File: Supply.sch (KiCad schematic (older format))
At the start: 22 parts, among them IC2 TPS65320C

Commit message: - updated project to 5.0.0 - added ignore file
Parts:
- B1: symbol MTC1 -> HSWR-V2-rescue:MTC1
- C27, C28, C30, C31, C32, C45, C46, C47, C48: symbol C -> Device:C
- C29, C49: symbol CP -> Device:CP
- D8, D9: symbol D_Schottky -> Device:D_Schottky
- IC2: symbol TPS65320C -> HSWR-V2-rescue:TPS65320C
- L1: symbol INDUCTOR -> HSWR-V2-rescue:INDUCTOR
- R39, R40, R41, R42, R43, R44: symbol R -> Device:R
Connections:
- wire segments 30 -> 38
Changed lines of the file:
@@
-EESchema Schematic File Version 2
-LIBS:HSWR V2-rescue
-LIBS:power
-LIBS:device
-LIBS:transistors
-LIBS:conn
-LIBS:linear
-LIBS:regul
-LIBS:74xx
-LIBS:cmos4000
-LIBS:adc-dac
-LIBS:memory
-LIBS:xilinx
-LIBS:microcontrollers
-LIBS:dsp
-LIBS:microchip
-LIBS:analog_switches
-LIBS:motorola
-LIBS:texas
-LIBS:intel
-LIBS:audio
-LIBS:interface
-LIBS:digital-audio
-LIBS:philips
-LIBS:display
-LIBS:cypress
-LIBS:siliconi
-LIBS:opto
-LIBS:atmel
-LIBS:contrib
-LIBS:valves
+EESchema Schematic File Version 4
 LIBS:HSWR V2-cache
-EELAYER 25 0
+EELAYER 26 0
 EELAYER END
 $Descr A4 11693 8268
@@
 $EndDescr
 $Comp
-L C C28
+L Device:C C28
 U 1 1 5757C618
 P 3350 3100
@@
 	3350 2800 3350 2950
 $Comp
-L GND #PWR052
+L power:GND #PWR052
 U 1 1 5757C686
 P 3350 3250
@@
 $EndComp
 $Comp
-L +12V #PWR053
+L power:+12V #PWR053
 U 1 1 5757C6C9
 P 3350 2800
@@
 Connection ~ 3350 2950
 $Comp
-L MTC1 B1
+L HSWR-V2-rescue:MTC1 B1
 U 1 1 5759A0C2
 P 2300 3150
@@
 $EndComp
 $Comp
-L +12VA #PWR054
+L power:+12VA #PWR054
 U 1 1 5759A1BD
 P 1350 2800
@@
 $EndComp
 Wire Wire Line
-	1350 2800 1350 3000
+	1350 2800 1350 2950
 Wire Wire Line
 	1350 2950 1650 2950
 $Comp
-L Earth #PWR055
+L power:Earth #PWR055
 U 1 1 5759A43B
 P 1350 3500
@@
 $EndComp
 Wire Wire Line
-	1350 3300 1350 3500
+	1350 3300 1350 3350
 Wire Wire Line
 	1350 3350 1650 3350
 $Comp
-L C C27
+L Device:C C27
 U 1 1 5759AB81
 P 1350 3150
@@
 Connection ~ 1350 3350
 $Comp
-L GND #PWR056
+L power:GND #PWR056
 U 1 1 5759B7CF
 P 2950 3350
@@
 $EndComp
 $Comp
-L TPS65320C IC2
+L HSWR-V2-rescue:TPS65320C IC2
 U 1 1 589B5162
 P 5100 3500
@@
 $EndComp
 $Comp
-L C C30
+L Device:C C30
 U 1 1 589B52B3
 P 3950 3100
@@
 $EndComp
 $Comp
-L CP C29
+L Device:CP C29
 U 1 1 589B52D8
 P 3650 3100
@@
 $EndComp
 Wire Wire Line
-	2950 2950 4350 2950
-Wire Wire Line
-	3350 3250 3350 3250
+	2950 2950 3350 2950
 Connection ~ 3950 2950
 Connection ~ 3650 2950
 $Comp
-L GND #PWR057
+L power:GND #PWR057
 U 1 1 589B5534
 P 3650 3250
@@
 $EndComp
 $Comp
-L GND #PWR058
+L power:GND #PWR058
 U 1 1 589B5551
 P 3950 3250
@@
 $EndComp
 Wire Wire Line
-	4350 2950 4350 3450
+	4350 2950 4350 3300
 Connection ~ 4350 3300
 Connection ~ 4350 2950
 $Comp
-L R R39
+L Device:R R39
 U 1 1 589B5713
 P 3900 4250
@@
 $EndComp
 $Comp
-L C C31
+L Device:C C31
 U 1 1 589B5758
 P 4150 4250
@@
 	3900 3950 3900 4100
 $Comp
-L GND #PWR059
+L power:GND #PWR059
 U 1 1 589B57C2
 P 3900 4400
@@
 $EndComp
 $Comp
-L GND #PWR060
+L power:GND #PWR060
 U 1 1 589B57E5
 P 4150 4400
@@
 $EndComp
 $Comp
-L GND #PWR061
+L power:GND #PWR061
 U 1 1 589B58C3
 P 4900 4400
@@
 $EndComp
 $Comp
-L GND #PWR062
+L power:GND #PWR062
 U 1 1 589B58E6
 P 5300 4400
@@
 $EndComp
 $Comp
-L R R42
+L Device:R R42
 U 1 1 589B5963
 P 6350 4100
@@
 $EndComp
 $Comp
-L R R41
+L Device:R R41
 U 1 1 589B59A7
 P 6200 4250
@@
 $EndComp
 $Comp
-L GND #PWR063
+L power:GND #PWR063
 U 1 1 589B5AA4
 P 6200 4400
@@
 	1    0    0    -1
 $EndComp
-Wire Wire Line
-	6200 4400 6200 4400
 Connection ~ 6200 4100
 Wire Wire Line
@@
 	6500 3750 6500 4100
 $Comp
-L C C47
+L Device:C C47
 U 1 1 589B5CE1
 P 6500 4250
@@
 $EndComp
 $Comp
-L GND #PWR064
+L power:GND #PWR064
 U 1 1 589B5D3A
 P 6500 4400
@@
 Connection ~ 6500 4100
 $Comp
-L +3V3 #PWR065
+L power:+3V3 #PWR065
 U 1 1 589B5D71
 P 6650 4100
@@
 $EndComp
 $Comp
-L R R40
+L Device:R R40
 U 1 1 589B6017
 P 6100 3500
@@
 $EndComp
 $Comp
-L C C45
+L Device:C C45
 U 1 1 589B6055
 P 6100 3650
@@
 $EndComp
 $Comp
-L C C46
+L Device:C C46
 U 1 1 589B6319
 P 6400 3500
@@
 Connection ~ 5850 3500
 $Comp
-L GND #PWR066
+L power:GND #PWR066
 U 1 1 589B655F
 P 6550 3500
@@
 $EndComp
 $Comp
-L R R43
+L Device:R R43
 U 1 1 589B6AE0
 P 7150 3400
@@
 $EndComp
 $Comp
-L R R44
+L Device:R R44
 U 1 1 589B6BD8
 P 7300 3250
@@
 $EndComp
 $Comp
-L GND #PWR067
+L power:GND #PWR067
 U 1 1 589B6C41
 P 7150 3550
@@
 	5850 3250 7150 3250
 $Comp
-L C C48
+L Device:C C48
 U 1 1 589B6CE4
 P 7450 3400
@@
 $EndComp
 $Comp
-L GND #PWR068
+L power:GND #PWR068
 U 1 1 589B6D8B
 P 7450 3550
@@
 $EndComp
 $Comp
-L GND #PWR069
+L power:GND #PWR069
 U 1 1 589B6DCC
 P 7700 3550
@@
 Connection ~ 7450 3250
 $Comp
-L D_Schottky D9
+L Device:D_Schottky D9
 U 1 1 589B7102
 P 6900 3450
@@
 $EndComp
 $Comp
-L GND #PWR070
+L power:GND #PWR070
 U 1 1 589B715E
 P 6900 3600
@@
 $EndComp
 Wire Wire Line
-	5850 3100 7000 3100
-$Comp
-L INDUCTOR L1
+	5850 3100 6150 3100
+$Comp
+L HSWR-V2-rescue:INDUCTOR L1
 U 1 1 589B8AC8
 P 7300 3100
@@
 $EndComp
 $Comp
-L C C32
+L Device:C C32
 U 1 1 589B8B47
 P 6000 2950
@@
 	6500 4100 6650 4100
 Wire Wire Line
-	7700 2500 7700 3250
+	7700 2500 7700 2600
 Wire Wire Line
 	6900 3300 6900 3100
@@
 Connection ~ 7700 3250
 $Comp
-L +5V #PWR071
+L power:+5V #PWR071
 U 1 1 589BAA8C
 P 7700 2500
@@
 Connection ~ 7700 2600
 $Comp
-L D_Schottky D8
+L Device:D_Schottky D8
 U 1 1 589BBCFD
 P 5850 4250
@@
 NRST
 $Comp
-L CP C49
+L Device:CP C49
 U 1 1 589C2A67
 P 7700 3400
@@
 Wire Wire Line
 	7600 3100 7700 3100
+Wire Wire Line
+	3350 2950 3650 2950
+Wire Wire Line
+	1350 2950 1350 3000
+Wire Wire Line
+	1350 3350 1350 3500
+Wire Wire Line
+	3950 2950 4350 2950
+Wire Wire Line
+	3650 2950 3950 2950
+Wire Wire Line
+	4350 3300 4350 3450
+Wire Wire Line
+	6150 3100 6900 3100
+Wire Wire Line
+	6900 3100 7000 3100
+Wire Wire Line
+	7700 3100 7700 3250
+Wire Wire Line
+	7700 2600 7700 3100
 $EndSCHEMATC

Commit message: - updated to VESC6 architecture - still some things to do in schematic
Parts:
- removed B1: MTC1, alexmod:MTC1, symbol HSWR-V2-rescue:MTC1
- removed C27, C28: 22u, Capacitors_SMD:C_1206, symbol Device:C
- removed C29: 100u 16V, Capacitors_ThroughHole:C_Radial_D6.3_L11.2_P2.5, symbol Device:CP
- removed C30, C47, C48: 10u, Capacitors_SMD:C_0805, symbol Device:C
- removed C31: 3n3, Capacitors_SMD:C_0805, symbol Device:C
- removed C32: 100n, Capacitors_SMD:C_0805, symbol Device:C
- removed C45: 10p, Capacitors_SMD:C_0805, symbol Device:C
- removed C46: 5n6, Capacitors_SMD:C_0805, symbol Device:C
- removed C49: 100u 6V3, Capacitors_ThroughHole:C_Radial_D6.3_L11.2_P2.5, symbol Device:CP
- removed D8, D9: D_Schottky, Diodes_SMD:SMA_Standard, symbol Device:D_Schottky
- removed IC2: TPS65320C, alexmod:TSSOP-14_4.4x5mm_Pitch0.65mm_EP, symbol HSWR-V2-rescue:TPS65320C
- removed L1: SRR6038-3R3Y, alexmod:SRR6038, symbol HSWR-V2-rescue:INDUCTOR
- removed R39: 52k3, Resistors_SMD:R_0805, symbol Device:R
- removed R40: 28k, Resistors_SMD:R_0805, symbol Device:R
- removed R41: 30k1, Resistors_SMD:R_0805, symbol Device:R
- removed R42, R44: 95k3, Resistors_SMD:R_0805, symbol Device:R
- removed R43: 18k2, Resistors_SMD:R_0805, symbol Device:R
- added NT1: Net-Tie_2, NetTie:NetTie-3_SMD_Pad0.5mm, symbol Device:Net-Tie_2
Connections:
- net labels added: GNDPWR
- net labels removed: +12V, +12VA, +3V3, +5V, Earth, NRST
- wire segments 38 -> 0

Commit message: - layout pretty much finished except PSU and maaaaybe R2D - started work on R2D with AD2S1205
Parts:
- NT1: footprint NetTie:NetTie-3_SMD_Pad0.5mm -> NetTie:NetTie-2_SMD_Pad2.0mm
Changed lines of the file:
@@
 $Descr A4 11693 8268
 encoding utf-8
-Sheet 4 7
+Sheet 4 9
 Title ""
 Date ""
@@
 F 0 "NT1" H 2800 5528 50  0000 C CNN
 F 1 "Net-Tie_2" H 2800 5437 50  0000 C CNN
-F 2 "NetTie:NetTie-3_SMD_Pad0.5mm" H 2800 5350 50  0001 C CNN
+F 2 "NetTie:NetTie-2_SMD_Pad2.0mm" H 2800 5350 50  0001 C CNN
 F 3 "~" H 2800 5350 50  0001 C CNN
 	1    2800 5350

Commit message: - removed R2D.sch - selected PSUs - finished layout
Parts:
- added C41, C42, C45, C46: 22u, Capacitor_SMD:C_0805_2012Metric, symbol Device:C
- added C43, C44: 100n, Capacitor_SMD:C_0805_2012Metric, symbol Device:C_Small
- added C47, C48: 2u2, Capacitor_SMD:C_0805_2012Metric, symbol Device:C_Small
- added IC6, IC7: JW5052C, Package_TO_SOT_SMD:TSOT-23-6, symbol Auktoralib:JW5052C
- added IC8: B1212S-2W, Converter_DCDC:Converter_DCDC_muRata_NMAxxxxSC_THT, symbol Auktoralib:DCDC_6pin
- added L1, L2: FCI201209F-4R7K, Inductor_SMD:L_0805_2012Metric, symbol Device:L
- added R44, R45: 100k, Resistor_SMD:R_0805_2012Metric, symbol Device:R_Small
- added R46: 110k, Resistor_SMD:R_0805_2012Metric, symbol Device:R_Small
- added R47: 15k, Resistor_SMD:R_0805_2012Metric, symbol Device:R_Small
- added R48: 49k9, Resistor_SMD:R_0805_2012Metric, symbol Device:R_Small
- added R49: 11k, Resistor_SMD:R_0805_2012Metric, symbol Device:R_Small
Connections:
- net labels added: +12V, +12VA, +3V3, +5V, Earth
- wire segments 0 -> 11
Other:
- moved on the sheet: NT1

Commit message: - corrected current filter resistors - adapted USB footprint - added 0.1% note to dc bus voltage divider
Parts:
- IC6, IC7: symbol Auktoralib:JW5052C -> HSWR-V2-rescue:JW5052C-Auktoralib
- IC8: symbol Auktoralib:DCDC_6pin -> HSWR-V2-rescue:DCDC_6pin-Auktoralib
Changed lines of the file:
@@
 $EndComp
 $Comp
-L Auktoralib:JW5052C IC7
+L HSWR-V2-rescue:JW5052C-Auktoralib IC7
 U 1 1 5C9E348B
 P 3850 5550
@@
 Connection ~ 5300 5450
 $Comp
-L Auktoralib:JW5052C IC6
+L HSWR-V2-rescue:JW5052C-Auktoralib IC6
 U 1 1 5C9E68F7
 P 3850 4150
@@
 $EndComp
 $Comp
-L Auktoralib:DCDC_6pin IC8
+L HSWR-V2-rescue:DCDC_6pin-Auktoralib IC8
 U 1 1 5C9F1AAA
 P 3850 2900

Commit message: - rescued schematic - added *.sch-bak to ignore - fixed bypass diode polarity - fixed PDEN being low - added 0R resistors instead of USB iso option - added caps to DCDC - added filter to VDDA
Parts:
- added C49, C51: 100u/16V, Capacitor_THT:CP_Radial_D6.3mm_P2.50mm, symbol Device:CP_Small
- C41: value 22u -> 22u/16V; symbol Device:C -> HSWR-V2-rescue:C-Device
- C42, C45, C46: value 22u -> 22u/6V3; symbol Device:C -> HSWR-V2-rescue:C-Device
- C43, C44, C47, C48: symbol Device:C_Small -> HSWR-V2-rescue:C_Small-Device
- IC6, IC7: symbol HSWR-V2-rescue:JW5052C-Auktoralib -> HSWR-V2-rescue:JW5052C-Auktoralib-HSWR-rescue
- IC8: symbol HSWR-V2-rescue:DCDC_6pin-Auktoralib -> HSWR-V2-rescue:DCDC_6pin-Auktoralib-HSWR-rescue
- L1, L2: symbol Device:L -> HSWR-V2-rescue:L-Device
- NT1: symbol Device:Net-Tie_2 -> HSWR-V2-rescue:Net-Tie_2-Device
- R44, R45, R46, R47, R48, R49: symbol Device:R_Small -> HSWR-V2-rescue:R_Small-Device
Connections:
- net +12V: now also C51.1
- net +12VA: now also C49.1
- net Earth: now also C49.2
- net GND: now also C51.2
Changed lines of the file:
@@
 EESchema Schematic File Version 4
-LIBS:HSWR V2-cache
-EELAYER 26 0
+EELAYER 30 0
 EELAYER END
 $Descr A4 11693 8268
@@
 $EndDescr
 $Comp
-L Device:Net-Tie_2 NT1
+L HSWR-V2-rescue:Net-Tie_2-Device NT1
 U 1 1 5C9BC448
 P 3850 6600
@@
 $EndComp
 $Comp
-L power:GND #PWR0121
+L HSWR-V2-rescue:GND-power #PWR0121
 U 1 1 5C9BC4AA
 P 3750 6600
@@
 $EndComp
 $Comp
-L power:GNDPWR #PWR0122
+L HSWR-V2-rescue:GNDPWR-power #PWR0122
 U 1 1 5C9BC4F1
 P 3950 6600
@@
 $EndComp
 $Comp
-L HSWR-V2-rescue:JW5052C-Auktoralib IC7
+L HSWR-V2-rescue:JW5052C-Auktoralib-HSWR-rescue IC7
 U 1 1 5C9E348B
 P 3850 5550
@@
 $EndComp
 $Comp
-L Device:C_Small C44
+L HSWR-V2-rescue:C_Small-Device C44
 U 1 1 5C9E3608
 P 4250 5350
@@
 $EndComp
 $Comp
-L Device:L L2
+L HSWR-V2-rescue:L-Device L2
 U 1 1 5C9E3F81
 P 4700 5450
@@
 Wire Wire Line
 	4550 5450 4250 5450
-Connection ~ 4250 5450
-$Comp
-L Device:C C46
+$Comp
+L HSWR-V2-rescue:C-Device C46
 U 1 1 5C9E3FDF
 P 5300 5600
 F 0 "C46" H 5415 5646 50  0000 L CNN
-F 1 "22u" H 5415 5555 50  0000 L CNN
+F 1 "22u/6V3" H 5415 5555 50  0000 L CNN
 F 2 "Capacitor_SMD:C_0805_2012Metric" H 5338 5450 50  0001 C CNN
 F 3 "~" H 5300 5600 50  0001 C CNN
@@
 $EndComp
 $Comp
-L Device:R_Small R48
+L HSWR-V2-rescue:R_Small-Device R48
 U 1 1 5C9E4149
 P 4850 5550
@@
 $EndComp
 $Comp
-L Device:R_Small R49
+L HSWR-V2-rescue:R_Small-Device R49
 U 1 1 5C9E4171
 P 4850 5750
@@
 Connection ~ 4850 5450
 $Comp
-L power:GND #PWR0182
+L HSWR-V2-rescue:GND-power #PWR0182
 U 1 1 5C9E41F1
 P 3850 6000
@@
 $EndComp
 $Comp
-L power:GND #PWR0183
+L HSWR-V2-rescue:GND-power #PWR0183
 U 1 1 5C9E4213
 P 4850 5850
@@
 $EndComp
 $Comp
-L power:GND #PWR0184
+L HSWR-V2-rescue:GND-power #PWR0184
 U 1 1 5C9E422E
 P 5300 5750
@@
 Connection ~ 4850 5650
 $Comp
-L Device:R_Small R45
+L HSWR-V2-rescue:R_Small-Device R45
 U 1 1 5C9E4723
 P 3450 5350
@@
 $EndComp
 $Comp
-L Device:C C42
+L HSWR-V2-rescue:C-Device C42
 U 1 1 5C9E4C14
 P 3150 5600
 F 0 "C42" H 3265 5646 50  0000 L CNN
-F 1 "22u" H 3265 5555 50  0000 L CNN
+F 1 "22u/6V3" H 3265 5555 50  0000 L CNN
 F 2 "Capacitor_SMD:C_0805_2012Metric" H 3188 5450 50  0001 C CNN
 F 3 "~" H 3150 5600 50  0001 C CNN
@@
 $EndComp
 $Comp
-L power:GND #PWR0185
+L HSWR-V2-rescue:GND-power #PWR0185
 U 1 1 5C9E4C52
 P 3150 5750
@@
 Wire Wire Line
 	3150 5250 3450 5250
-Connection ~ 3450 5250
-$Comp
-L power:+3V3 #PWR0186
+$Comp
+L HSWR-V2-rescue:+3V3-power #PWR0186
 U 1 1 5C9E5148
 P 5300 5450
@@
 Connection ~ 5300 5450
 $Comp
-L HSWR-V2-rescue:JW5052C-Auktoralib IC6
+L HSWR-V2-rescue:JW5052C-Auktoralib-HSWR-rescue IC6
 U 1 1 5C9E68F7
 P 3850 4150
@@
 $EndComp
 $Comp
-L Device:C_Small C43
+L HSWR-V2-rescue:C_Small-Device C43
 U 1 1 5C9E68FD
 P 4250 3950
@@
 $EndComp
 $Comp
-L Device:L L1
+L HSWR-V2-rescue:L-Device L1
 U 1 1 5C9E6903
 P 4700 4050
@@
 Wire Wire Line
 	4550 4050 4250 4050
-Connection ~ 4250 4050
-$Comp
-L Device:C C45
+$Comp
+L HSWR-V2-rescue:C-Device C45
 U 1 1 5C9E690B
 P 5300 4200
 F 0 "C45" H 5415 4246 50  0000 L CNN
-F 1 "22u" H 5415 4155 50  0000 L CNN
+F 1 "22u/6V3" H 5415 4155 50  0000 L CNN
 F 2 "Capacitor_SMD:C_0805_2012Metric" H 5338 4050 50  0001 C CNN
 F 3 "~" H 5300 4200 50  0001 C CNN
@@
 $EndComp
 $Comp
-L Device:R_Small R46
+L HSWR-V2-rescue:R_Small-Device R46
 U 1 1 5C9E6911
 P 4850 4150
@@
 $EndComp
 $Comp
-L Device:R_Small R47
+L HSWR-V2-rescue:R_Small-Device R47
 U 1 1 5C9E6917
 P 4850 4350
@@
 Connection ~ 4850 4050
 $Comp
-L power:GND #PWR0187
+L HSWR-V2-rescue:GND-power #PWR0187
 U 1 1 5C9E691F
 P 3850 4600
@@
 $EndComp
 $Comp
-L power:GND #PWR0188
+L HSWR-V2-rescue:GND-power #PWR0188
 U 1 1 5C9E6925
 P 4850 4450
@@
 $EndComp
 $Comp
-L power:GND #PWR0189
+L HSWR-V2-rescue:GND-power #PWR0189
 U 1 1 5C9E692B
 P 5300 4350
@@
 Connection ~ 4850 4250
 $Comp
-L Device:R_Small R44
+L HSWR-V2-rescue:R_Small-Device R44
 U 1 1 5C9E6933
 P 3450 3950
@@
 $EndComp
 $Comp
-L Device:C C41
+L HSWR-V2-rescue:C-Device C41
 U 1 1 5C9E6939
 P 3150 4200
 F 0 "C41" H 3265 4246 50  0000 L CNN
-F 1 "22u" H 3265 4155 50  0000 L CNN
+F 1 "22u/16V" H 3265 4155 50  0000 L CNN
 F 2 "Capacitor_SMD:C_0805_2012Metric" H 3188 4050 50  0001 C CNN
 F 3 "~" H 3150 4200 50  0001 C CNN
@@
 $EndComp
 $Comp
-L power:GND #PWR0190
+L HSWR-V2-rescue:GND-power #PWR0190
 U 1 1 5C9E693F
 P 3150 4350
@@
 Wire Wire Line
 	3150 3850 3450 3850
-Connection ~ 3450 3850
-$Comp
-L power:+12V #PWR0191
+$Comp
+L HSWR-V2-rescue:+12V-power #PWR0191
 U 1 1 5C9E6948
 P 3150 3850
@@
 Connection ~ 3150 3850
 $Comp
-L power:+5V #PWR0192
+L HSWR-V2-rescue:+5V-power #PWR0192
 U 1 1 5C9E6DAC
 P 5300 4050
@@
 Connection ~ 5300 4050
 $Comp
-L power:+5V #PWR0193
+L HSWR-V2-rescue:+5V-power #PWR0193
 U 1 1 5C9E7E71
 P 3150 5250
@@
 Connection ~ 3150 5250
 $Comp
-L Device:C_Small C47
+L HSWR-V2-rescue:C_Small-Device C47
 U 1 1 5C9EB58E
 P 3450 2900
@@
 $EndComp
 $Comp
-L Device:C_Small C48
+L HSWR-V2-rescue:C_Small-Device C48
 U 1 1 5C9EB75E
 P 4250 2800
@@
 $EndComp
 $Comp
-L power:Earth #PWR0195
+L HSWR-V2-rescue:Earth-power #PWR0195
 U 1 1 5C9EBAE0
 P 3450 3000
@@
 $EndComp
 $Comp
-L power:GND #PWR0196
+L HSWR-V2-rescue:GND-power #PWR0196
 U 1 1 5C9EBC32
 P 4250 3100
@@
 $EndComp
 $Comp
-L power:+12VA #PWR0197
+L HSWR-V2-rescue:+12VA-power #PWR0197
 U 1 1 5C9F009D
 P 3450 2800
@@
 $EndComp
 $Comp
-L power:+12V #PWR0198
+L HSWR-V2-rescue:+12V-power #PWR0198
 U 1 1 5C9F02AD
 P 4250 2700
@@
 $EndComp
 $Comp
-L HSWR-V2-rescue:DCDC_6pin-Auktoralib IC8
+L HSWR-V2-rescue:DCDC_6pin-Auktoralib-HSWR-rescue IC8
 U 1 1 5C9F1AAA
 P 3850 2900
@@
 	1    0    0    -1
 $EndComp
-Connection ~ 3450 2800
-Connection ~ 3450 3000
-Connection ~ 4250 2700
 Wire Wire Line
 	4250 2900 4250 3100
 Connection ~ 4250 2900
 Connection ~ 4250 3100
+$Comp
+L Device:CP_Small C51
+U 1 1 5E227FE9
+P 4600 2800
+F 0 "C51" H 4688 2846 50  0000 L CNN
+F 1 "100u/16V" H 4688 2755 50  0000 L CNN
+F 2 "Capacitor_THT:CP_Radial_D6.3mm_P2.50mm" H 4600 2800 50  0001 C CNN
+F 3 "~" H 4600 2800 50  0001 C CNN
+	1    4600 2800
+	1    0    0    -1
+$EndComp
+Wire Wire Line
+	4600 2700 4250 2700
+Connection ~ 4250 2700
+Wire Wire Line
+	4600 2900 4250 2900
+$Comp
+L Device:CP_Small C49
+U 1 1 5E22948F
+P 3100 2900
+F 0 "C49" H 3200 2950 50  0000 L CNN
+F 1 "100u/16V" H 3200 2850 50  0000 L CNN
+F 2 "Capacitor_THT:CP_Radial_D6.3mm_P2.50mm" H 3100 2900 50  0001 C CNN
+F 3 "~" H 3100 2900 50  0001 C CNN
+	1    3100 2900
+	-1   0    0    -1
+$EndComp
+Wire Wire Line
+	3450 2800 3100 2800
+Connection ~ 3450 2800
+Wire Wire Line
+	3450 3000 3100 3000
+Connection ~ 3450 3000
+Connection ~ 3450 3850
+Connection ~ 4250 4050
+Connection ~ 3450 5250
+Connection ~ 4250 5450
 $EndSCHEMATC

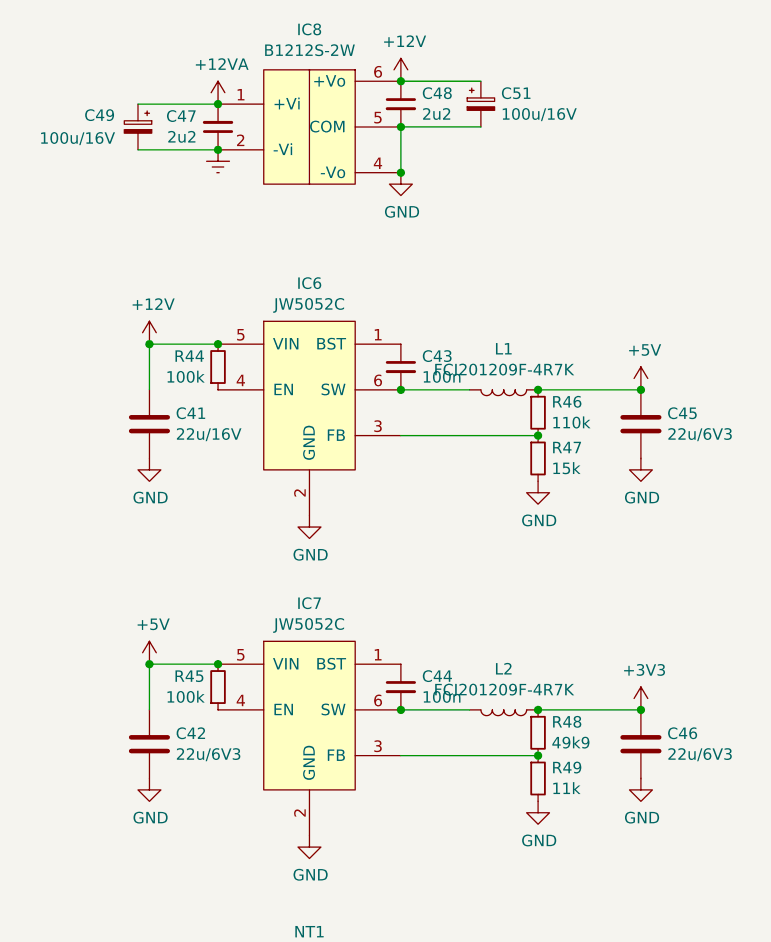
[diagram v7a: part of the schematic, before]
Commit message: - changed CSA for Hall effect sensors - updated power stage layout
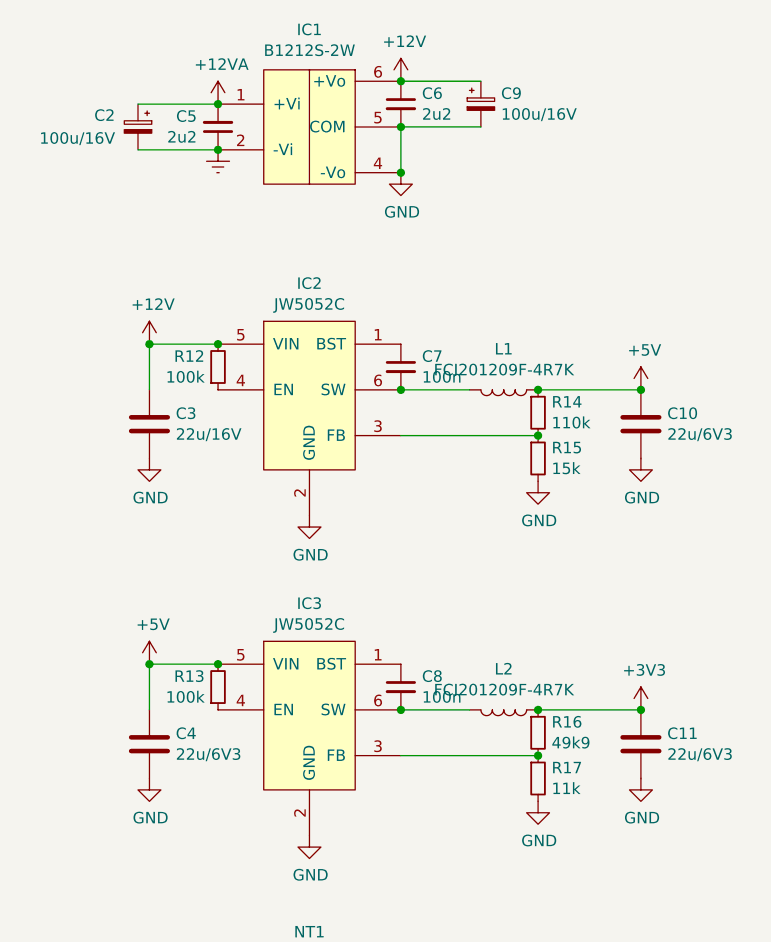
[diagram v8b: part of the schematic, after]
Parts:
- renumbered C45 to C10, C46 to C11, C49 to C2, C41 to C3, C42 to C4, C47 to C5, C48 to C6, C43 to C7, C44 to C8, C51 to C9, IC8 to IC1, IC6 to IC2, IC7 to IC3, R44 to R12, R45 to R13, R46 to R14, R47 to R15, R48 to R16, R49 to R17
